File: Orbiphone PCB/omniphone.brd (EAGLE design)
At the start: 80 x 80 mm, 46 parts

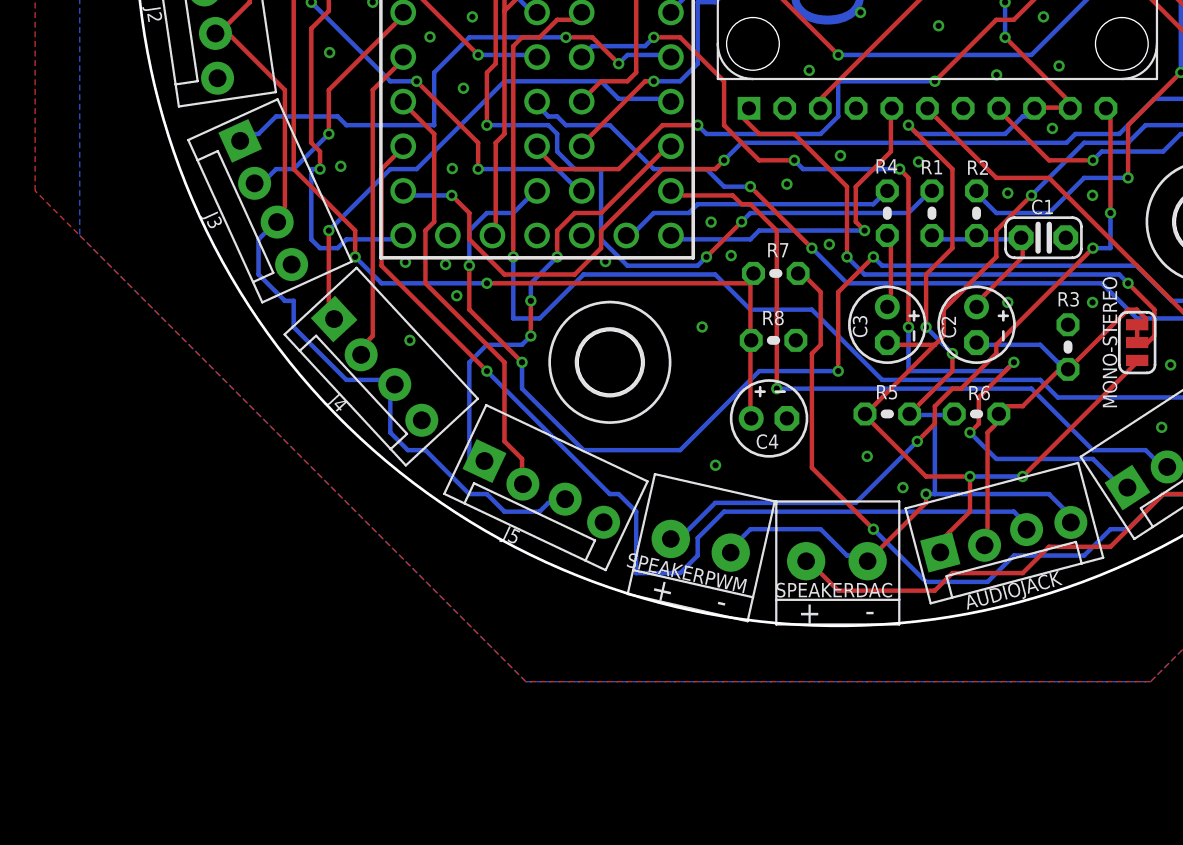
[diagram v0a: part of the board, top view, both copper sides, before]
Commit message: added speaker and headphone fixes
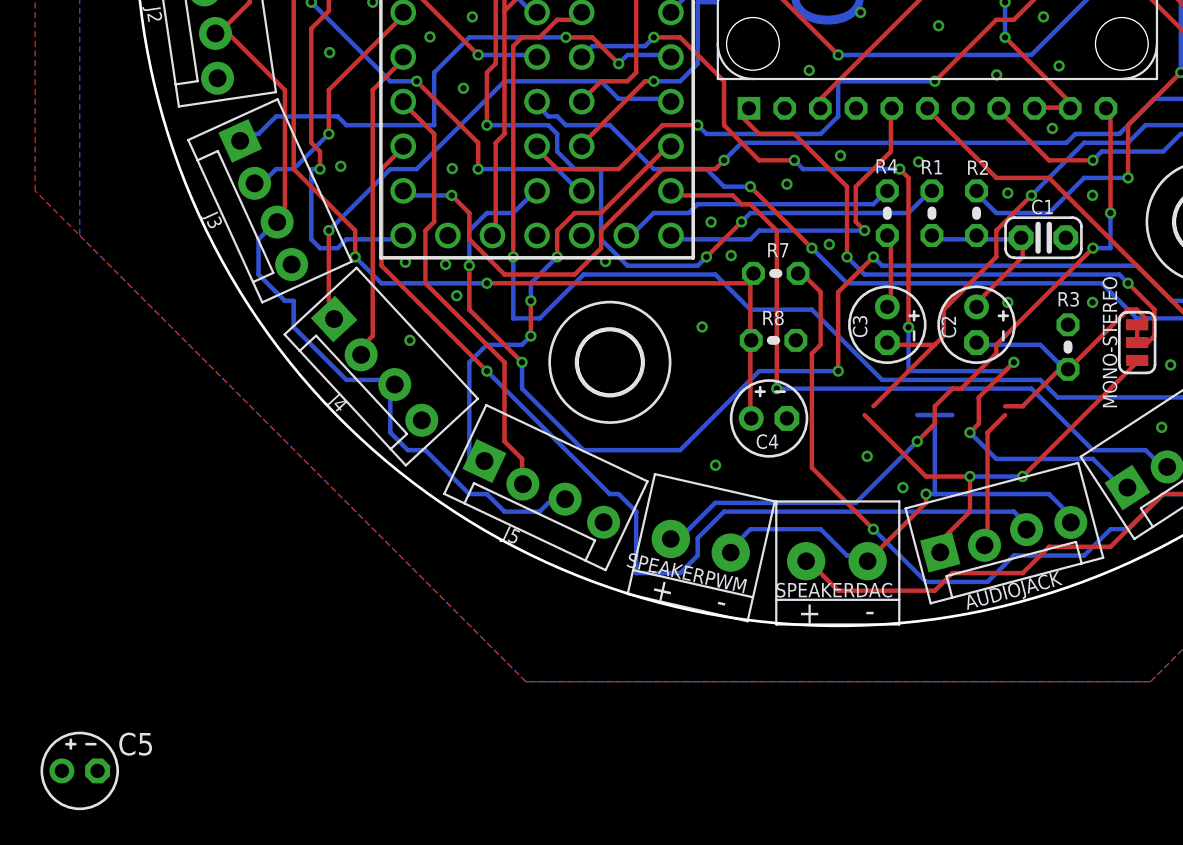
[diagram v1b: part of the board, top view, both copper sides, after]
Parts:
- removed R5, R6: 10k, adafruit:0204V
- added C5: 22uF, adafruit:E2-4
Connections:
- new net L-: AMP.L-, SPEAKERDAC.-
- new net R-: AMP.R-, SPEAKERPWM.-
- net AGND: no longer AMP.L-, AMP.R-, AUDIOJACK.4, R5.1, R6.1, SPEAKERDAC.-, SPEAKERPWM.-
- net AUDIODAC: no longer R5.2
- net AUDIOPWM: now also C5.+; no longer R6.2
- net GND: now also AUDIOJACK.4, C5.-
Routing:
- net AGND: track 179.0 -> 117.9 mm, vias 11 -> 7
- net GND: track 0.00 -> 20.6 mm, vias 69 -> 70
- net L-: track 0.00 -> 10.7 mm
- net AUDIOPWM: track 26.8 -> 25.8 mm
- net AUDIODAC: track 94.7 -> 93.9 mm

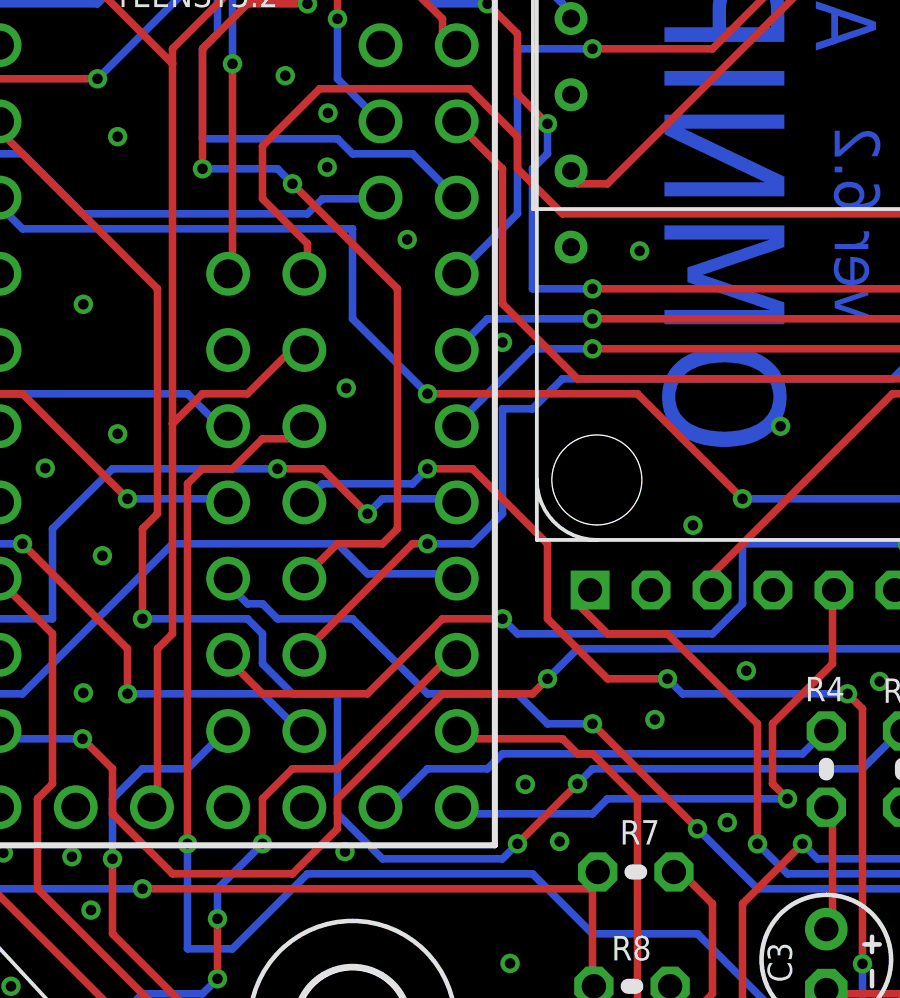
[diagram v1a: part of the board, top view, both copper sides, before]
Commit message: changed the ampswitch as 13 doesn't work with its led on it
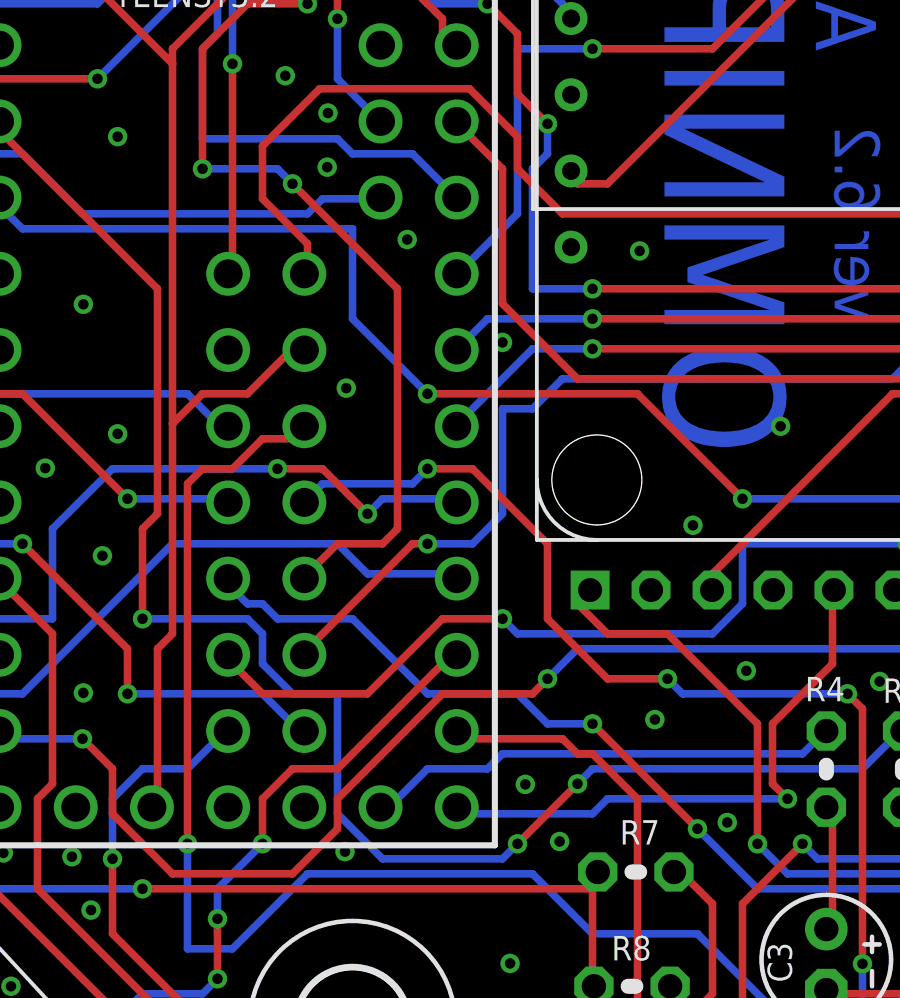
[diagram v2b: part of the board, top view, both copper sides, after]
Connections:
- net AMPSWITCH: now also TEENSY3.2.21/A7; no longer TEENSY3.2.13
- net POTSWITCH: no longer TEENSY3.2.21/A7
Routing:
- net POTSWITCH: track 79.6 -> 78.9 mm
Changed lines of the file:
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@@
 <signal name="AMPSWITCH">
 <contactref element="AMP" pad="SW"/>
-<contactref element="TEENSY3.2" pad="13"/>
 <wire x1="3" y1="-13" x2="3" y2="-11" width="0.254" layer="1"/>
 <wire x1="1" y1="-15" x2="3" y2="-13" width="0.254" layer="1"/>
@@
 <wire x1="-9.5" y1="-18" x2="-5" y2="-18" width="0.254" layer="16"/>
 <wire x1="3" y1="-11" x2="3.048" y2="-10.541" width="0.254" layer="1"/>
-<wire x1="-9.5" y1="-18" x2="-9.525" y2="-17.78" width="0.254" layer="16"/>
 <via x="1.5" y="-17.5" extent="1-16" drill="0.35"/>
+<contactref element="TEENSY3.2" pad="21/A7"/>
+<wire x1="-9.525" y1="2.54" x2="3.048" y2="-10.541" width="0" layer="19" extent="1-1"/>
 </signal>
 <signal name="ENC0">
@@
 <signal name="POTSWITCH">
 <contactref element="T/POWER" pad="3"/>
-<contactref element="TEENSY3.2" pad="21/A7"/>
 <wire x1="-7" y1="35" x2="-7" y2="35.5" width="0.254" layer="1"/>
 <wire x1="-7.5" y1="34.5" x2="-7" y2="35" width="0.254" layer="1"/>
@@
 <wire x1="-10" y1="3" x2="-11" y2="4" width="0.254" layer="16"/>
 <wire x1="-7" y1="35.5" x2="-7.493" y2="35.433" width="0.254" layer="1"/>
-<wire x1="-10" y1="3" x2="-9.525" y2="2.54" width="0.254" layer="16"/>
 <via x="-8" y="34.5" extent="1-16" drill="0.35"/>
 </signal>

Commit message: preparations for powerswitch modification
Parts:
- removed T/POWER: JUMPER-SMT_3_1-NC_TRACE_SILK, SparkFun-Jumpers:SMT-JUMPER_3_1-NC_TRACE_SILK
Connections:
- removed net N$4: POT.2, T/POWER.2
- removed net POTSWITCH: T/POWER.3
- net POWERENABLE: now also POT.2; no longer T/POWER.1
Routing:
- net POTSWITCH: track 78.9 -> 0.00 mm, vias 1 -> 0
- net N$4: track 11.1 -> 0.00 mm
- net POWERENABLE: track 74.2 -> 84.2 mm
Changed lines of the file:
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@@
 <attribute name="NAME" x="-12.11675625" y="-36.6161625" size="0.8128" layer="25" rot="SR347.2"/>
-</element>
-<element name="T/POWER" library="SparkFun-Jumpers" library_urn="urn:adsk.eagle:library:528" package="SMT-JUMPER_3_1-NC_TRACE_SILK" package3d_urn="urn:adsk.eagle:package:39288/1" value="JUMPER-SMT_3_1-NC_TRACE_SILK" x="-7.493" y="36.449" smashed="yes" rot="R270">
-<attribute name="NAME" x="-5.461" y="36.576" size="0.8128" layer="25" ratio="20" rot="SR90" align="bottom-center"/>
 </element>
 <element name="BATTERY" library="ArvidLibrary" package="1X2-3.5MM" package3d_urn="urn:adsk.eagle:package:6240635/1" value="SPEAKERTERMINAL-3.5MM" x="11.049" y="34.671" smashed="yes" rot="R163">
@@
 <signal name="POWERENABLE">
 <contactref element="U$3" pad="EN"/>
-<contactref element="T/POWER" pad="1"/>
 <wire x1="-2.5" y1="33" x2="-7" y2="37.5" width="0.254" layer="1"/>
 <wire x1="2" y1="28.5" x2="-2.5" y2="33" width="0.254" layer="16"/>
@@
 <wire x1="-4.5" y1="3" x2="3.5" y2="11" width="0.254" layer="1"/>
 <wire x1="-5.5" y1="3" x2="-4.5" y2="3" width="0.254" layer="1"/>
-<wire x1="-7" y1="37.5" x2="-7.493" y2="37.465" width="0.254" layer="1"/>
 <wire x1="-5.5" y1="3" x2="-5.715" y2="3.429" width="0.254" layer="1"/>
 <via x="-2.5" y="33" extent="1-16" drill="0.35"/>
@@
 <via x="20.5" y="23" extent="1-16" drill="0.35"/>
 <via x="6" y="11" extent="1-16" drill="0.35"/>
+<contactref element="POT" pad="2"/>
+<wire x1="-6" y1="35.5" x2="-7" y2="36.5" width="0.254" layer="1"/>
+<wire x1="-6" y1="35" x2="-6" y2="35.5" width="0.254" layer="1"/>
+<wire x1="-8" y1="33" x2="-6" y2="35" width="0.254" layer="1"/>
+<wire x1="-12" y1="33" x2="-8" y2="33" width="0.254" layer="1"/>
+<wire x1="-13" y1="34" x2="-12" y2="33" width="0.254" layer="1"/>
+<wire x1="-13" y1="34" x2="-12.613225" y2="34.1511875" width="0.254" layer="1"/>
+<wire x1="-7" y1="37.5" x2="-7" y2="36.5" width="0" layer="19" extent="1-1"/>
 </signal>
 <signal name="L+">
@@
 <via x="-11.5" y="32" extent="1-16" drill="0.35"/>
 </signal>
-<signal name="POTSWITCH">
-<contactref element="T/POWER" pad="3"/>
-<wire x1="-7" y1="35" x2="-7" y2="35.5" width="0.254" layer="1"/>
-<wire x1="-7.5" y1="34.5" x2="-7" y2="35" width="0.254" layer="1"/>
-<wire x1="-8" y1="34.5" x2="-7.5" y2="34.5" width="0.254" layer="1"/>
-<wire x1="-8" y1="37" x2="-8" y2="34.5" width="0.254" layer="16"/>
-<wire x1="-10.5" y1="37" x2="-8" y2="37" width="0.254" layer="16"/>
-<wire x1="-11.5" y1="36" x2="-10.5" y2="37" width="0.254" layer="16"/>
-<wire x1="-13.5" y1="36" x2="-11.5" y2="36" width="0.254" layer="16"/>
-<wire x1="-15.5" y1="34" x2="-13.5" y2="36" width="0.254" layer="16"/>
-<wire x1="-17.5" y1="34" x2="-15.5" y2="34" width="0.254" layer="16"/>
-<wire x1="-20" y1="31.5" x2="-17.5" y2="34" width="0.254" layer="16"/>
-<wire x1="-21.5" y1="31.5" x2="-20" y2="31.5" width="0.254" layer="16"/>
-<wire x1="-33" y1="20" x2="-21.5" y2="31.5" width="0.254" layer="16"/>
-<wire x1="-33" y1="17.5" x2="-33" y2="20" width="0.254" layer="16"/>
-<wire x1="-35.5" y1="15" x2="-33" y2="17.5" width="0.254" layer="16"/>
-<wire x1="-35.5" y1="12" x2="-35.5" y2="15" width="0.254" layer="16"/>
-<wire x1="-26.5" y1="12" x2="-35.5" y2="12" width="0.254" layer="16"/>
-<wire x1="-26" y1="11.5" x2="-26.5" y2="12" width="0.254" layer="16"/>
-<wire x1="-23.5" y1="11.5" x2="-26" y2="11.5" width="0.254" layer="16"/>
-<wire x1="-23" y1="11" x2="-23.5" y2="11.5" width="0.254" layer="16"/>
-<wire x1="-18.5" y1="11" x2="-23" y2="11" width="0.254" layer="16"/>
-<wire x1="-17.5" y1="10" x2="-18.5" y2="11" width="0.254" layer="16"/>
-<wire x1="-17.5" y1="8" x2="-17.5" y2="10" width="0.254" layer="16"/>
-<wire x1="-18" y1="7.5" x2="-17.5" y2="8" width="0.254" layer="16"/>
-<wire x1="-18" y1="4.5" x2="-18" y2="7.5" width="0.254" layer="16"/>
-<wire x1="-13.5" y1="4.5" x2="-18" y2="4.5" width="0.254" layer="16"/>
-<wire x1="-13" y1="4" x2="-13.5" y2="4.5" width="0.254" layer="16"/>
-<wire x1="-11" y1="4" x2="-13" y2="4" width="0.254" layer="16"/>
-<wire x1="-10" y1="3" x2="-11" y2="4" width="0.254" layer="16"/>
-<wire x1="-7" y1="35.5" x2="-7.493" y2="35.433" width="0.254" layer="1"/>
-<via x="-8" y="34.5" extent="1-16" drill="0.35"/>
-</signal>
 <signal name="VIN">
 <contactref element="TEENSY3.2" pad="VIN"/>
@@
 <via x="0.5" y="-19" extent="1-16" drill="0.35"/>
 </signal>
-<signal name="N$4">
-<contactref element="POT" pad="2"/>
-<contactref element="T/POWER" pad="2"/>
-<wire x1="-6" y1="35.5" x2="-7" y2="36.5" width="0.254" layer="1"/>
-<wire x1="-6" y1="35" x2="-6" y2="35.5" width="0.254" layer="1"/>
-<wire x1="-8" y1="33" x2="-6" y2="35" width="0.254" layer="1"/>
-<wire x1="-12" y1="33" x2="-8" y2="33" width="0.254" layer="1"/>
-<wire x1="-13" y1="34" x2="-12" y2="33" width="0.254" layer="1"/>
-<wire x1="-7" y1="36.5" x2="-7.493" y2="36.449" width="0.254" layer="1"/>
-<wire x1="-13" y1="34" x2="-12.613225" y2="34.1511875" width="0.254" layer="1"/>
-</signal>
 <signal name="BATSENSOR">
